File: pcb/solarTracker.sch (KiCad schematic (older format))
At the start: 31 parts, among them U1 74HC4052, U2 STM32F071CBT6

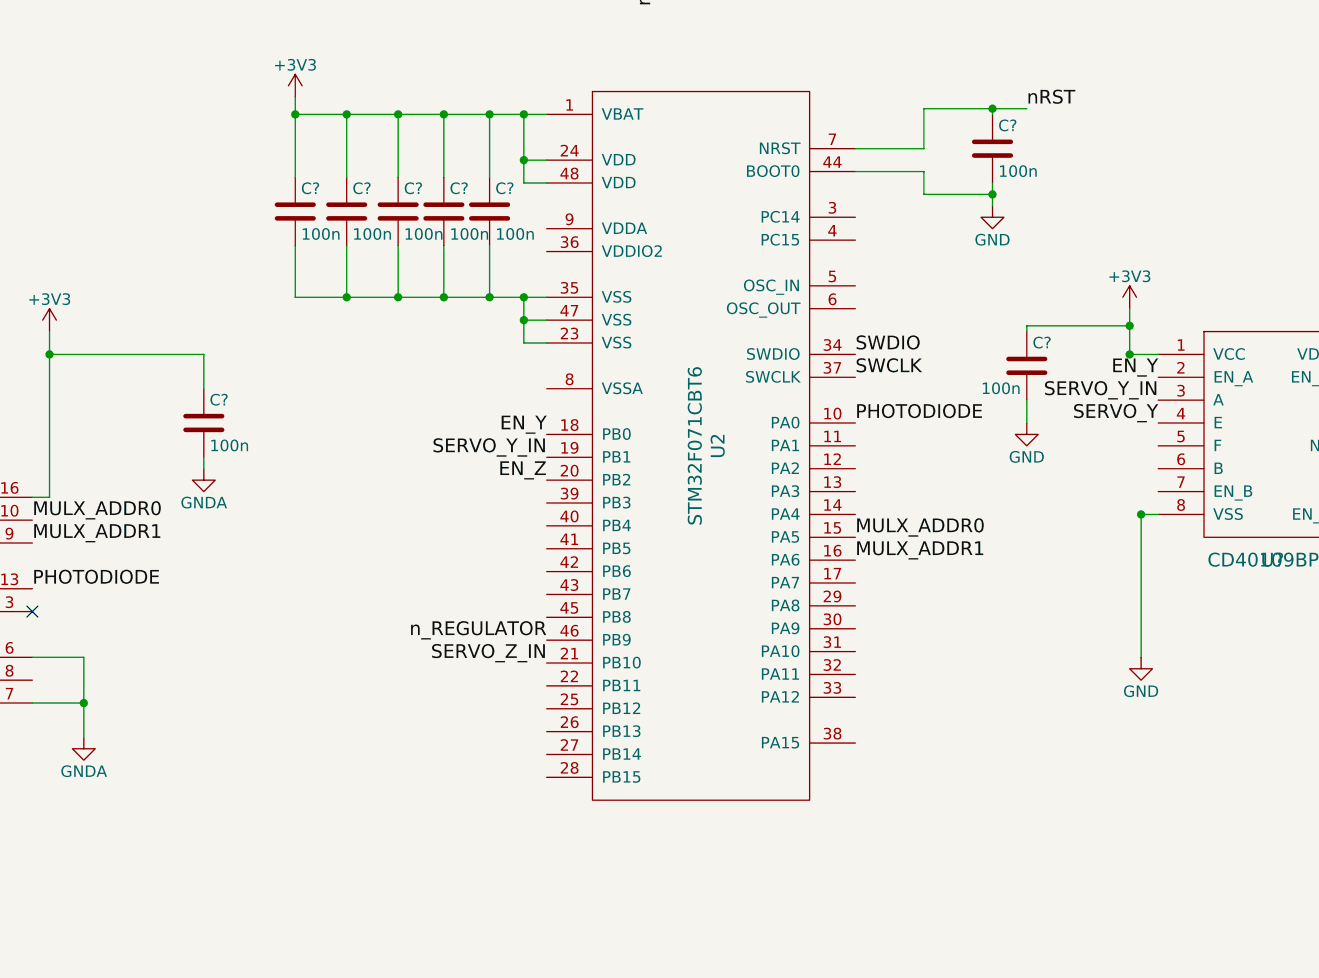
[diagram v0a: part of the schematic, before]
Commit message: add breakout header to interface with dev board
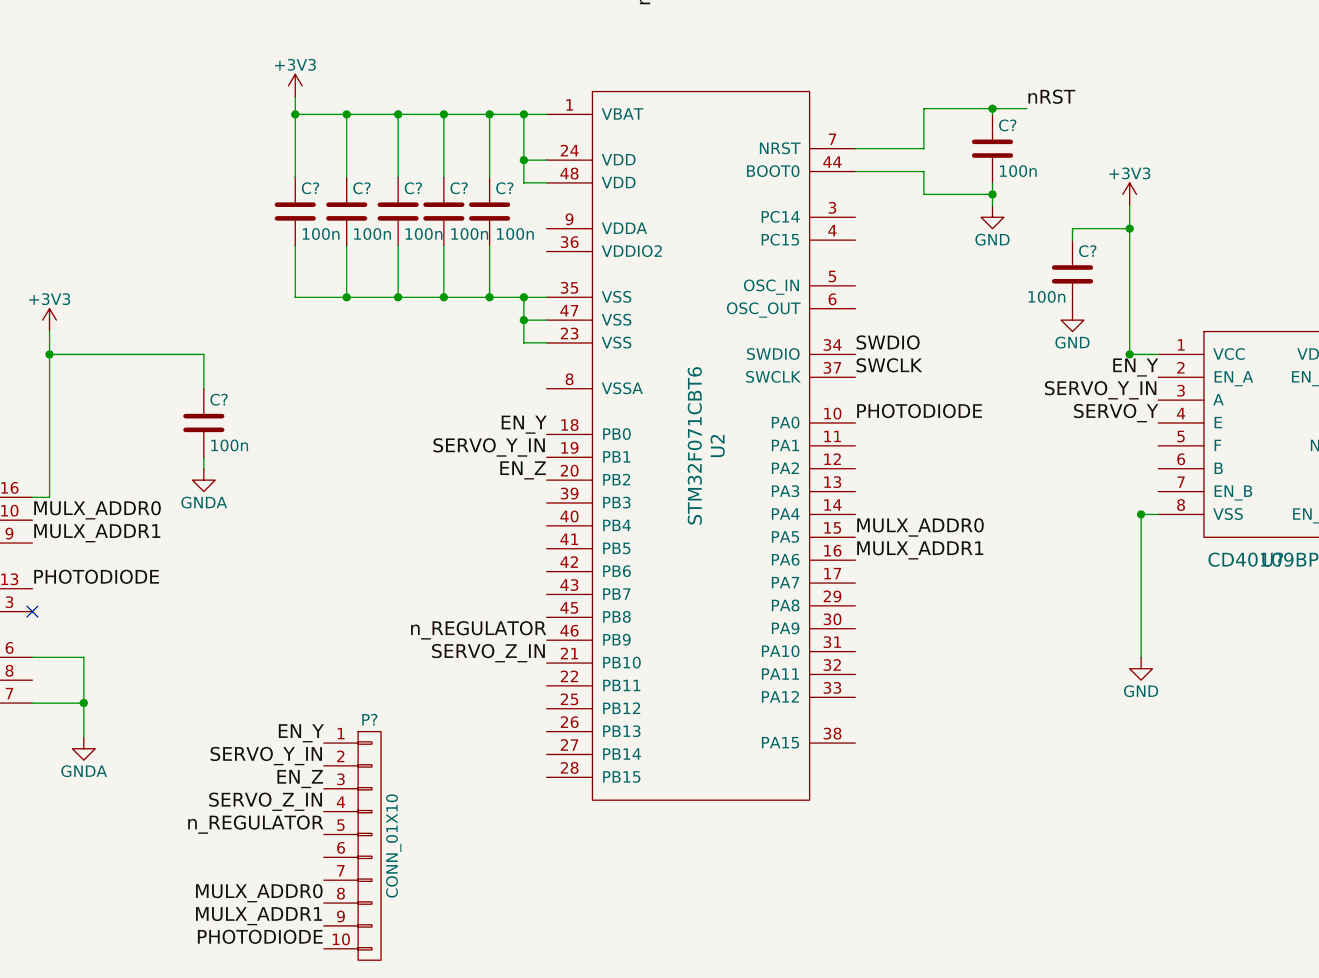
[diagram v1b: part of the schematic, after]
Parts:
- added P?: CONN_01X10, symbol CONN_01X10
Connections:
- net EN_Y: now also P?.1 (P1)
- net EN_Z: now also P?.3 (P3)
- net MULX_ADDR0: now also P?.8 (P8)
- net MULX_ADDR1: now also P?.9 (P9)
- net PHOTODIODE: now also P?.10 (P10)
- net SERVO_Y_IN: now also P?.2 (P2)
- net SERVO_Z_IN: now also P?.4 (P4)
- net n_REGULATOR: now also P?.5 (P5)
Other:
- moved on the sheet: C?
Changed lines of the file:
@@
 L +3V3 #PWR?
 U 1 1 587112C7
-P 8725 4325
-F 0 "#PWR?" H 8725 4175 50  0001 C CNN
-F 1 "+3V3" H 8725 4465 50  0000 C CNN
-F 2 "" H 8725 4325 60  0000 C CNN
-F 3 "" H 8725 4325 60  0000 C CNN
-	1    8725 4325
+P 8725 3875
+F 0 "#PWR?" H 8725 3725 50  0001 C CNN
+F 1 "+3V3" H 8725 4015 50  0000 C CNN
+F 2 "" H 8725 3875 60  0000 C CNN
+F 3 "" H 8725 3875 60  0000 C CNN
+	1    8725 3875
 	1    0    0    -1
 $EndComp
@@
 	9200 2150 9200 2125
 Wire Wire Line
-	8725 4325 8725 4400
-Wire Wire Line
-	8725 4400 8725 4525
+	8725 3875 8725 3975
+Wire Wire Line
+	8725 3975 8725 4525
 Wire Wire Line
 	9950 4275 9950 4325
@@
 L C C?
 U 1 1 5871CFBA
-P 8275 4575
-F 0 "C?" H 8300 4675 50  0000 L CNN
-F 1 "100n" H 8075 4475 50  0000 L CNN
-F 2 "" H 8313 4425 50  0000 C CNN
-F 3 "" H 8275 4575 50  0000 C CNN
-F 4 "Farnell" H 8275 4575 60  0001 C CNN "Supplier"
-F 5 "2496944" H 8275 4575 60  0001 C CNN "Order No"
-	1    8275 4575
+P 8475 4175
+F 0 "C?" H 8500 4275 50  0000 L CNN
+F 1 "100n" H 8275 4075 50  0000 L CNN
+F 2 "" H 8513 4025 50  0000 C CNN
+F 3 "" H 8475 4175 50  0000 C CNN
+F 4 "Farnell" H 8475 4175 60  0001 C CNN "Supplier"
+F 5 "2496944" H 8475 4175 60  0001 C CNN "Order No"
+	1    8475 4175
 	1    0    0    -1
 $EndComp
@@
 L GND #PWR?
 U 1 1 5871E17C
-P 8275 4825
-F 0 "#PWR?" H 8275 4575 50  0001 C CNN
-F 1 "GND" H 8275 4675 50  0000 C CNN
-F 2 "" H 8275 4825 60  0000 C CNN
-F 3 "" H 8275 4825 60  0000 C CNN
-	1    8275 4825
-	1    0    0    -1
-$EndComp
-Wire Wire Line
-	8275 4725 8275 4825
-Wire Wire Line
-	8275 4425 8275 4400
-Wire Wire Line
-	8275 4400 8725 4400
-Connection ~ 8725 4400
+P 8475 4325
+F 0 "#PWR?" H 8475 4075 50  0001 C CNN
+F 1 "GND" H 8475 4175 50  0000 C CNN
+F 2 "" H 8475 4325 60  0000 C CNN
+F 3 "" H 8475 4325 60  0000 C CNN
+	1    8475 4325
+	1    0    0    -1
+$EndComp
+Wire Wire Line
+	8475 4325 8475 4325
+Wire Wire Line
+	8475 4025 8475 3975
+Connection ~ 8725 3975
 Wire Wire Line
 	8725 4525 8850 4525
@@
 	1    0    0    -1
 $EndComp
+Wire Wire Line
+	8475 3975 8725 3975
+$Comp
+L CONN_01X10 P?
+U 1 1 5872A5A1
+P 5400 6675
+F 0 "P?" H 5400 7225 50  0000 C CNN
+F 1 "CONN_01X10" V 5500 6675 50  0000 C CNN
+F 2 "" H 5400 6675 50  0000 C CNN
+F 3 "" H 5400 6675 50  0000 C CNN
+	1    5400 6675
+	1    0    0    -1
+$EndComp
+Text Label 5200 6225 2    60   ~ 0
+EN_Y
+Text Label 5200 6325 2    60   ~ 0
+SERVO_Y_IN
+Text Label 5200 6425 2    60   ~ 0
+EN_Z
+Text Label 5200 6525 2    60   ~ 0
+SERVO_Z_IN
+Text Label 5200 6625 2    60   ~ 0
+n_REGULATOR
+Text Label 5200 7125 2    60   ~ 0
+PHOTODIODE
+Text Label 5200 6925 2    60   ~ 0
+MULX_ADDR0
+Text Label 5200 7025 2    60   ~ 0
+MULX_ADDR1
 $EndSCHEMATC

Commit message: fix µcu farnell code
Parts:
- added P?: CONN_01X02, symbol CONN_01X02
- U12: renamed from U?; Order No (none) -> 1741425; Supplier (none) -> Farnell
- U2: Order No 2376483 -> 2432093
- gave numbers to parts that had none: 27
- renumbered SERVO_Y to SERVO_Y1, SERVO_Z to SERVO_Z1
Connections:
- net +6V: now also P?.1 (P1)
- net GND: now also P?.2 (P2)

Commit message: footprint generation, chibiOS and chibiOS-servo libraries
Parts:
- removed C23, C24, C27, C7: 100n, symbol C
- removed U1: 74HC4052, symbol 74HC4052
- removed U11: LM2596, symbol LM2577
- added C? (x4): 100n, Capacitors_SMD:C_0805_HandSoldering, symbol C
- added U?: LM2596, solartracker:LM2596, symbol LM2596
- added U?: 74HC4052, Housings_SOIC:SOIC-16_3.9x9.9mm_Pitch1.27mm, symbol 74HC4052
- C19: footprint (none) -> Capacitors_ThroughHole:C_Radial_D8_L11.5_P3.5
- C22, C26: footprint (none) -> Capacitors_SMD:C_0805_HandSoldering
- C25: footprint (none) -> Capacitors_ThroughHole:C_Radial_D12.5_L25_P5
- D1: footprint (none) -> Diodes_ThroughHole:Diode_DO-201AD_Horizontal_RM15
- L1: footprint (none) -> solartracker:PE-53934SNLT
- R21, R22: footprint (none) -> Resistors_SMD:R_0805_HandSoldering
- U12: footprint (none) -> solartracker:TSSOP-16-CD40190BPW
- U2: footprint (none) -> solartracker:LQFP-48
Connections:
- net +3V3: now also C?.1, C?.1, U?.16 (VCC)
- net +6V: now also C?.1
- net +BATT: now also U?.1 (Vin)
- net GND: now also C22.2, C?.2, C?.2, C?.2, U?.3 (GND)
- net GNDA: now also C?.2, U?.6 (\ENB), U?.7 (VEE), U?.8 (GND)
- net MULX_ADDR0: now also U?.10 (S0)
- net MULX_ADDR1: now also U?.9 (S1)
- net PHOTODIODE: now also U?.13 (1Z)
- net nRST: now also C?.1
- net n_REGULATOR: now also U?.5 (ON/OFF)
- net photodiode0/DIO: now also U?.12 (1Y0)
- net photodiode1/DIO: now also U?.14 (1Y1)
- net photodiode2/DIO: now also U?.15 (1Y2)
- net photodiode3/DIO: now also U?.11 (1Y3)
- net at D1.1 (K), L1.1: now also U?.2 (Output)
- net at C26.2, R21.2, R22.1: now also U?.4 (FB)

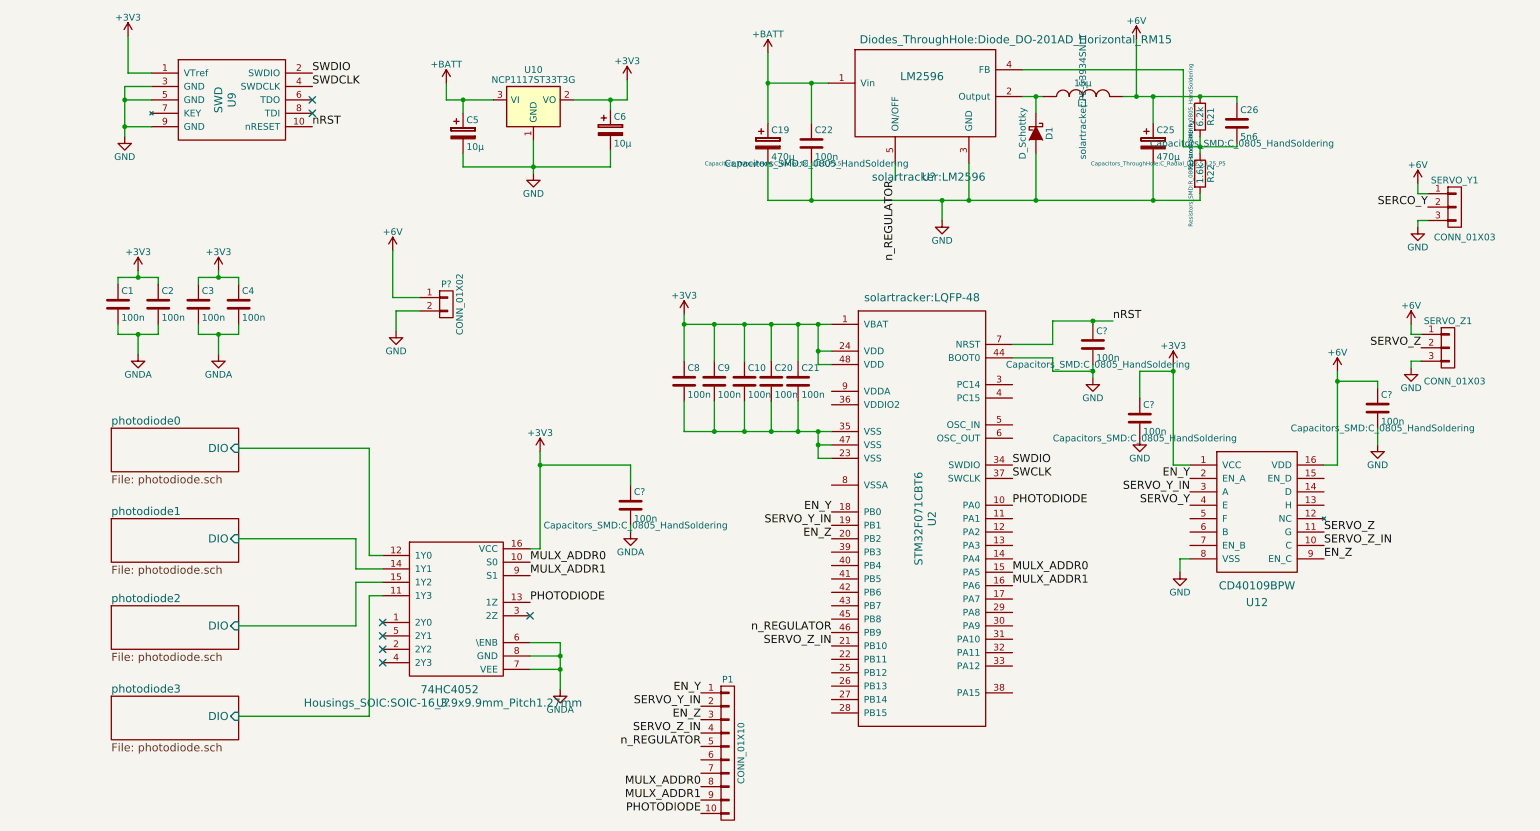
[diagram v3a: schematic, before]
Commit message: Changes to board, add footprints
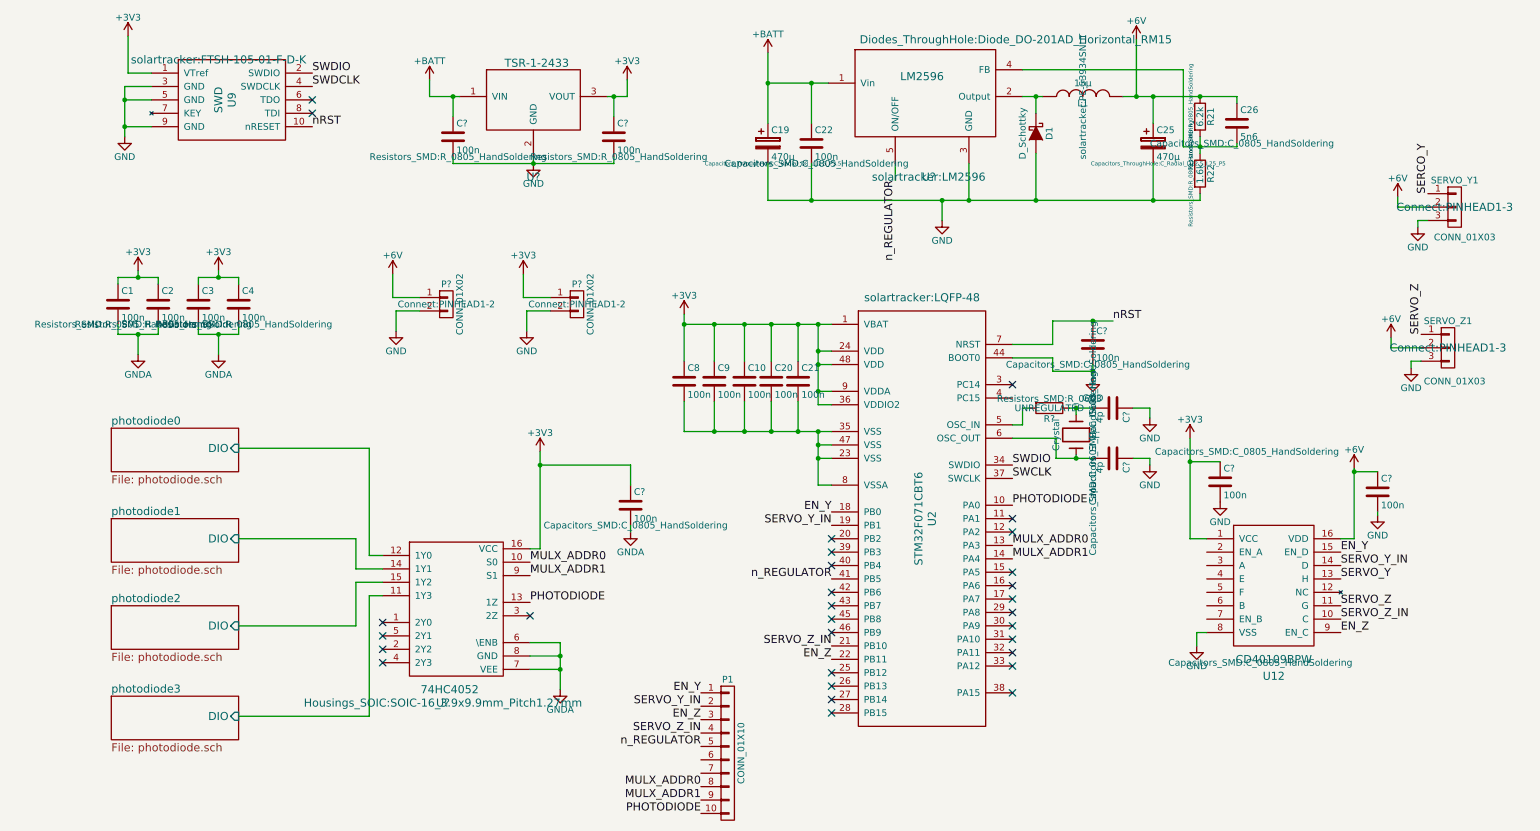
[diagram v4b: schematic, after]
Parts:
- removed C5, C6: 10µ, symbol CP
- removed U10: NCP1117ST33T3G, TO_SOT_Packages_SMD:SOT-223, symbol NCP1117ST33T3G
- added C? (x2): 4p, Capacitors_SMD:C_0603_HandSoldering, symbol C
- added C? (x2): 100n, Resistors_SMD:R_0805_HandSoldering, symbol C
- added P?: CONN_01X02, Connect:PINHEAD1-2, symbol CONN_01X02
- added R?: UNREGULATED, Resistors_SMD:R_0603, symbol R
- added U?: TSR-1-2433, solartracker:TSR12433, symbol TSR-1-2433
- added Y?: Crystal, symbol Crystal
- C1, C2, C4: footprint (none) -> Resistors_SMD:R_0805_HandSoldering
- P?: footprint (none) -> Connect:PINHEAD1-2
- SERVO_Y1, SERVO_Z1: footprint (none) -> Connect:PINHEAD1-3
- U9: footprint (none) -> solartracker:FTSH-105-01-F-D-K
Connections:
- net +3V3: now also U2.36 (VDDIO2), U2.9 (VDDA), C?.1, P?.1 (P1), U?.3 (VOUT)
- net +6V: now also SERVO_Y1.2 (P2), SERVO_Z1.2 (P2); no longer SERVO_Y1.1 (P1), SERVO_Z1.1 (P1)
- net +BATT: now also C?.1, U?.1 (VIN)
- net EN_Y: now also U12.15 (EN_D); no longer U12.2 (EN_A)
- net EN_Z: now also U2.22 (PB11); no longer U2.20 (PB2)
- net GND: now also C?.1, C?.1, C?.2, C?.2, P?.2 (P2), U?.2 (GND)
- net MULX_ADDR0: now also U2.13 (PA3); no longer U2.15 (PA5)
- net MULX_ADDR1: now also U2.14 (PA4); no longer U2.16 (PA6)
- net SERCO_Y: now also SERVO_Y1.1 (P1); no longer SERVO_Y1.2 (P2)
- net SERVO_Y: now also U12.13 (H); no longer U12.4 (E)
- net SERVO_Y_IN: now also U12.14 (D); no longer U12.3 (A)
- net SERVO_Z: now also SERVO_Z1.1 (P1); no longer SERVO_Z1.2 (P2)
- net n_REGULATOR: now also U2.41 (PB5); no longer U2.46 (PB9)
- net at C10.2, C20.2, C21.2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: now also U2.8 (VSSA)
- net at U2.5 (OSC_IN): now also R?.2
- net at U2.6 (OSC_OUT): now also C?.2, Y?.2
- new net: C?.2, R?.1, Y?.1
- no-connect marks 7 -> 30
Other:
- moved on the sheet: C?, U12
